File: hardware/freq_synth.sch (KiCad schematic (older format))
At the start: 13 parts

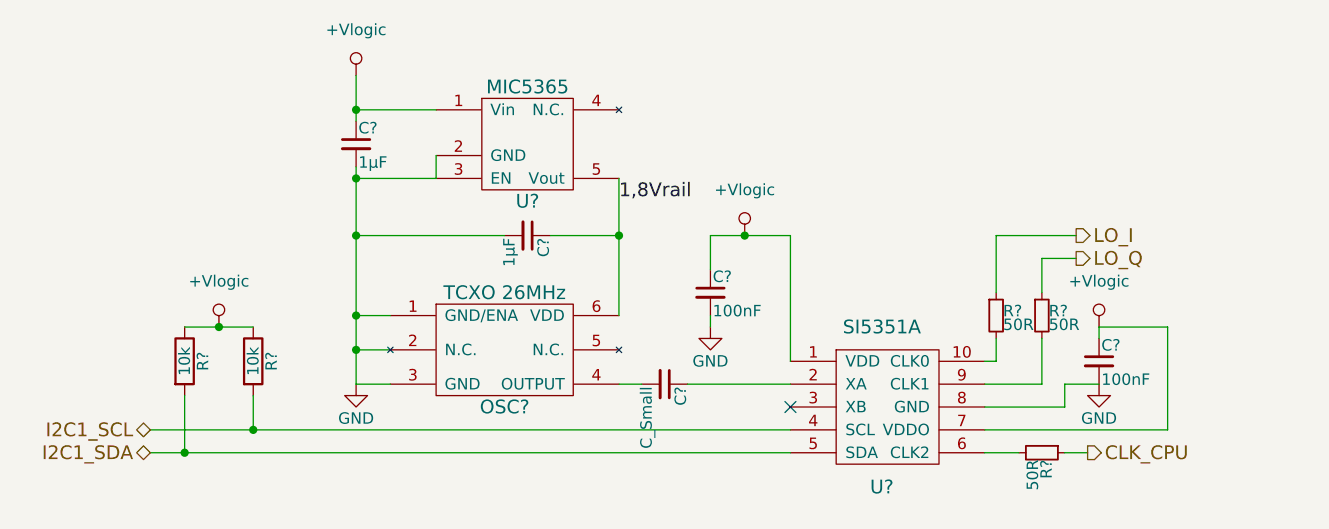
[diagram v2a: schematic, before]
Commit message: Added RX chain. also modified and cleand up other schemas
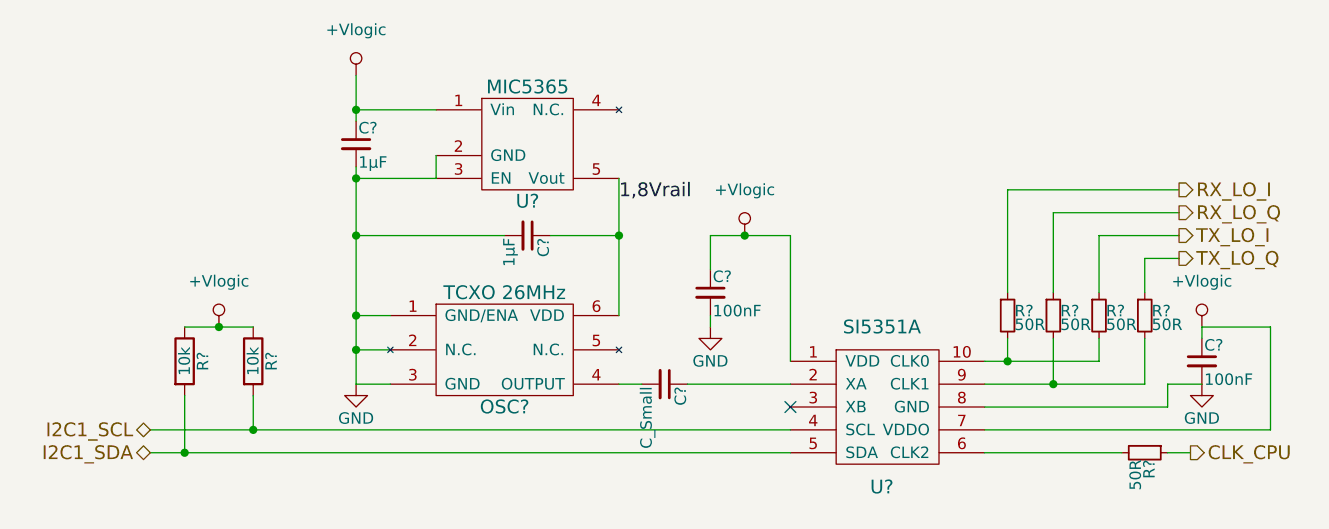
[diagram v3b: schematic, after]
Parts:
- added R? (x2): 50R, symbol R_Small
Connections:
- net at R?.2, U?.10 (CLK0): now also R?.2
- net at R?.2, U?.9 (CLK1): now also R?.2
- net LO_I renamed TX_LO_I
- net LO_Q renamed TX_LO_Q
- new net RX_LO_I: R?.1
- new net RX_LO_Q: R?.1
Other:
- moved on the sheet: C?, R?
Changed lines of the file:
@@
 $Descr A4 11693 8268
 encoding utf-8
-Sheet 2 5
+Sheet 2 7
 Title "Frequency synthesizer for LOs and CPU clock generation"
 Date "2016-09-22"
@@
 $EndDescr
 Wire Wire Line
-	7450 4500 7550 4500
-Wire Wire Line
-	7100 4500 7250 4500
-Wire Wire Line
-	7150 3550 7150 3800
-Wire Wire Line
-	7500 3550 7150 3550
-Wire Wire Line
-	7350 3650 7350 3800
-Wire Wire Line
-	7500 3650 7350 3650
-Wire Wire Line
-	7150 4100 7150 4000
-Wire Wire Line
-	7100 4100 7150 4100
-Wire Wire Line
-	7350 4200 7350 4000
-Wire Wire Line
-	7100 4200 7350 4200
+	7900 4500 8000 4500
+Wire Wire Line
+	7100 4500 7700 4500
+Wire Wire Line
+	7600 3550 7600 3800
+Wire Wire Line
+	7950 3550 7600 3550
+Wire Wire Line
+	7800 3650 7800 3800
+Wire Wire Line
+	7950 3650 7800 3650
+Wire Wire Line
+	7600 4100 7600 4000
+Wire Wire Line
+	7100 4100 7600 4100
+Wire Wire Line
+	7800 4200 7800 4000
+Wire Wire Line
+	7100 4200 7800 4200
 Connection ~ 3600 4500
 Connection ~ 3900 4400
 Wire Wire Line
-	7600 3950 7600 4000
-Wire Wire Line
-	7600 3950 7900 3950
-Wire Wire Line
-	7450 4200 7450 4300
+	8050 3950 8050 4000
+Wire Wire Line
+	8050 3950 8350 3950
+Wire Wire Line
+	7900 4200 7900 4300
 Connection ~ 4350 3000
 Connection ~ 4350 3550
 Wire Wire Line
-	5000 3550 4350 3550
+	4350 3550 5000 3550
 Connection ~ 5500 3550
 Wire Wire Line
@@
 	6250 3550 6250 4100
 Wire Wire Line
-	7900 3950 7900 4400
-Wire Wire Line
-	7900 4400 7100 4400
-Wire Wire Line
-	7450 4300 7100 4300
-Wire Wire Line
-	7450 4200 7600 4200
+	8350 3950 8350 4400
+Wire Wire Line
+	8350 4400 7100 4400
+Wire Wire Line
+	7900 4300 7100 4300
+Wire Wire Line
+	7900 4200 8050 4200
 Wire Wire Line
 	5900 3950 5900 3900
-Text HLabel 7550 4500 2    60   Output ~ 0
+Text HLabel 8000 4500 2    60   Output ~ 0
 CLK_CPU
 $Comp
 L R_Small R?
 U 1 1 57E319F9
-P 7350 4500
-F 0 "R?" H 7380 4520 50  0000 L CNN
-F 1 "50R" H 7380 4460 50  0000 L CNN
-F 2 "" H 7350 4500 50  0000 C CNN
-F 3 "" H 7350 4500 50  0000 C CNN
-	1    7350 4500
+P 7800 4500
+F 0 "R?" H 7830 4520 50  0000 L CNN
+F 1 "50R" H 7830 4460 50  0000 L CNN
+F 2 "" H 7800 4500 50  0000 C CNN
+F 3 "" H 7800 4500 50  0000 C CNN
+	1    7800 4500
 	0    1    1    0
 $EndComp
@@
 L R_Small R?
 U 1 1 57E31A00
-P 7150 3900
-F 0 "R?" H 7180 3920 50  0000 L CNN
-F 1 "50R" H 7180 3860 50  0000 L CNN
-F 2 "" H 7150 3900 50  0000 C CNN
-F 3 "" H 7150 3900 50  0000 C CNN
-	1    7150 3900
+P 7600 3900
+F 0 "R?" H 7630 3920 50  0000 L CNN
+F 1 "50R" H 7630 3860 50  0000 L CNN
+F 2 "" H 7600 3900 50  0000 C CNN
+F 3 "" H 7600 3900 50  0000 C CNN
+	1    7600 3900
 	1    0    0    -1
 $EndComp
@@
 L R_Small R?
 U 1 1 57E31A07
-P 7350 3900
-F 0 "R?" H 7380 3920 50  0000 L CNN
-F 1 "50R" H 7380 3860 50  0000 L CNN
-F 2 "" H 7350 3900 50  0000 C CNN
-F 3 "" H 7350 3900 50  0000 C CNN
-	1    7350 3900
-	1    0    0    -1
-$EndComp
-Text HLabel 7500 3550 2    60   Output ~ 0
-LO_I
-Text HLabel 7500 3650 2    60   Output ~ 0
-LO_Q
+P 7800 3900
+F 0 "R?" H 7830 3920 50  0000 L CNN
+F 1 "50R" H 7830 3860 50  0000 L CNN
+F 2 "" H 7800 3900 50  0000 C CNN
+F 3 "" H 7800 3900 50  0000 C CNN
+	1    7800 3900
+	1    0    0    -1
+$EndComp
+Text HLabel 7950 3550 2    60   Output ~ 0
+TX_LO_I
+Text HLabel 7950 3650 2    60   Output ~ 0
+TX_LO_Q
 Text HLabel 3450 4400 0    60   BiDi ~ 0
 I2C1_SCL
@@
 1,8Vrail
 $Comp
-L +Vlogic #PWR?
+L +Vlogic #PWR02
 U 1 1 57E31A13
 P 4350 2850
-F 0 "#PWR?" H 4350 2650 50  0001 C CNN
+F 0 "#PWR02" H 4350 2650 50  0001 C CNN
 F 1 "+Vlogic" H 4350 3050 50  0000 C CNN
 F 2 "" H 4350 2850 50  0000 C CNN
@@
 $EndComp
 $Comp
-L GND #PWR?
+L GND #PWR03
 U 1 1 57E31A2E
 P 4350 4200
-F 0 "#PWR?" H 4350 3950 50  0001 C CNN
+F 0 "#PWR03" H 4350 3950 50  0001 C CNN
 F 1 "GND" H 4350 4050 50  0000 C CNN
 F 2 "" H 4350 4200 50  0000 C CNN
@@
 $EndComp
 $Comp
-L +Vlogic #PWR?
+L +Vlogic #PWR04
 U 1 1 57E31A3B
 P 3750 3950
-F 0 "#PWR?" H 3750 3750 50  0001 C CNN
+F 0 "#PWR04" H 3750 3750 50  0001 C CNN
 F 1 "+Vlogic" H 3750 4150 50  0000 C CNN
 F 2 "" H 3750 3950 50  0000 C CNN
@@
 $EndComp
 $Comp
-L +Vlogic #PWR?
+L +Vlogic #PWR05
 U 1 1 57E31A41
-P 7600 3950
-F 0 "#PWR?" H 7600 3750 50  0001 C CNN
-F 1 "+Vlogic" H 7600 4150 50  0000 C CNN
-F 2 "" H 7600 3950 50  0000 C CNN
-F 3 "" H 7600 3950 50  0000 C CNN
-	1    7600 3950
+P 8050 3950
+F 0 "#PWR05" H 8050 3750 50  0001 C CNN
+F 1 "+Vlogic" H 8050 4150 50  0000 C CNN
+F 2 "" H 8050 3950 50  0000 C CNN
+F 3 "" H 8050 3950 50  0000 C CNN
+	1    8050 3950
 	1    0    0    -1
 $EndComp
@@
 $EndComp
 $Comp
-L +Vlogic #PWR?
+L +Vlogic #PWR06
 U 1 1 57E31A5D
 P 6050 3550
-F 0 "#PWR?" H 6050 3350 50  0001 C CNN
+F 0 "#PWR06" H 6050 3350 50  0001 C CNN
 F 1 "+Vlogic" H 6050 3750 50  0000 C CNN
 F 2 "" H 6050 3550 50  0000 C CNN
@@
 L C_Small C?
 U 1 1 57E31A63
-P 7600 4100
-F 0 "C?" H 7610 4170 50  0000 L CNN
-F 1 "100nF" H 7610 4020 50  0000 L CNN
-F 2 "" H 7600 4100 50  0000 C CNN
-F 3 "" H 7600 4100 50  0000 C CNN
-	1    7600 4100
+P 8050 4100
+F 0 "C?" H 8060 4170 50  0000 L CNN
+F 1 "100nF" H 8060 4020 50  0000 L CNN
+F 2 "" H 8050 4100 50  0000 C CNN
+F 3 "" H 8050 4100 50  0000 C CNN
+	1    8050 4100
 	1    0    0    -1
 $EndComp
@@
 $EndComp
 $Comp
-L GND #PWR?
+L GND #PWR07
 U 1 1 57E31A71
 P 5900 3950
-F 0 "#PWR?" H 5900 3700 50  0001 C CNN
+F 0 "#PWR07" H 5900 3700 50  0001 C CNN
 F 1 "GND" H 5900 3800 50  0000 C CNN
 F 2 "" H 5900 3950 50  0000 C CNN
@@
 $EndComp
 $Comp
-L GND #PWR?
+L GND #PWR08
 U 1 1 57E31A77
-P 7600 4200
-F 0 "#PWR?" H 7600 3950 50  0001 C CNN
-F 1 "GND" H 7600 4050 50  0000 C CNN
-F 2 "" H 7600 4200 50  0000 C CNN
-F 3 "" H 7600 4200 50  0000 C CNN
-	1    7600 4200
+P 8050 4200
+F 0 "#PWR08" H 8050 3950 50  0001 C CNN
+F 1 "GND" H 8050 4050 50  0000 C CNN
+F 2 "" H 8050 4200 50  0000 C CNN
+F 3 "" H 8050 4200 50  0000 C CNN
+	1    8050 4200
 	1    0    0    -1
 $EndComp
@@
 	1    0    0    -1
 $EndComp
+$Comp
+L R_Small R?
+U 1 1 57E545D0
+P 7400 3900
+F 0 "R?" H 7430 3920 50  0000 L CNN
+F 1 "50R" H 7430 3860 50  0000 L CNN
+F 2 "" H 7400 3900 50  0000 C CNN
+F 3 "" H 7400 3900 50  0000 C CNN
+	1    7400 3900
+	1    0    0    -1
+$EndComp
+$Comp
+L R_Small R?
+U 1 1 57E54652
+P 7200 3900
+F 0 "R?" H 7230 3920 50  0000 L CNN
+F 1 "50R" H 7230 3860 50  0000 L CNN
+F 2 "" H 7200 3900 50  0000 C CNN
+F 3 "" H 7200 3900 50  0000 C CNN
+	1    7200 3900
+	1    0    0    -1
+$EndComp
+Wire Wire Line
+	7200 4100 7200 4000
+Connection ~ 7200 4100
+Wire Wire Line
+	7400 4200 7400 4000
+Connection ~ 7400 4200
+Text HLabel 7950 3450 2    60   Output ~ 0
+RX_LO_Q
+Text HLabel 7950 3350 2    60   Output ~ 0
+RX_LO_I
+Wire Wire Line
+	7400 3800 7400 3450
+Wire Wire Line
+	7400 3450 7950 3450
+Wire Wire Line
+	7200 3800 7200 3350
+Wire Wire Line
+	7200 3350 7950 3350
 $EndSCHEMATC

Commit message: Added annotation so willing prove readers can reference components more easily
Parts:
- gave numbers to parts that had none: 15
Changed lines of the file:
@@
 CLK_CPU
 $Comp
-L R_Small R?
+L R_Small R207
 U 1 1 57E319F9
 P 7800 4500
-F 0 "R?" H 7830 4520 50  0000 L CNN
+F 0 "R207" H 7830 4520 50  0000 L CNN
 F 1 "50R" H 7830 4460 50  0000 L CNN
 F 2 "" H 7800 4500 50  0000 C CNN
@@
 $EndComp
 $Comp
-L R_Small R?
+L R_Small R205
 U 1 1 57E31A00
 P 7600 3900
-F 0 "R?" H 7630 3920 50  0000 L CNN
+F 0 "R205" H 7630 3920 50  0000 L CNN
 F 1 "50R" H 7630 3860 50  0000 L CNN
 F 2 "" H 7600 3900 50  0000 C CNN
@@
 $EndComp
 $Comp
-L R_Small R?
+L R_Small R206
 U 1 1 57E31A07
 P 7800 3900
-F 0 "R?" H 7830 3920 50  0000 L CNN
+F 0 "R206" H 7830 3920 50  0000 L CNN
 F 1 "50R" H 7830 3860 50  0000 L CNN
 F 2 "" H 7800 3900 50  0000 C CNN
@@
 1,8Vrail
 $Comp
-L +Vlogic #PWR02
+L +Vlogic #PWR202
 U 1 1 57E31A13
 P 4350 2850
-F 0 "#PWR02" H 4350 2650 50  0001 C CNN
+F 0 "#PWR202" H 4350 2650 50  0001 C CNN
 F 1 "+Vlogic" H 4350 3050 50  0000 C CNN
 F 2 "" H 4350 2850 50  0000 C CNN
@@
 $EndComp
 $Comp
-L C_Small C?
+L C_Small C202
 U 1 1 57E31A19
 P 5100 3550
-F 0 "C?" H 5110 3620 50  0000 L CNN
+F 0 "C202" H 5110 3620 50  0000 L CNN
 F 1 "1µF" H 5110 3470 50  0000 L CNN
 F 2 "" H 5100 3550 50  0000 C CNN
@@
 $EndComp
 $Comp
-L C_Small C?
+L C_Small C201
 U 1 1 57E31A20
 P 4350 3150
-F 0 "C?" H 4360 3220 50  0000 L CNN
+F 0 "C201" H 4360 3220 50  0000 L CNN
 F 1 "1µF" H 4360 3070 50  0000 L CNN
 F 2 "" H 4350 3150 50  0000 C CNN
@@
 $EndComp
 $Comp
-L LDO U?
+L LDO U201
 U 1 1 57E31A27
 P 5100 3100
-F 0 "U?" H 5100 2800 60  0000 C CNN
+F 0 "U201" H 5100 2800 60  0000 C CNN
 F 1 "MIC5365" H 5100 3300 60  0000 C CNN
 F 2 "" H 5100 3050 60  0001 C CNN
@@
 $EndComp
 $Comp
-L GND #PWR03
+L GND #PWR203
 U 1 1 57E31A2E
 P 4350 4200
-F 0 "#PWR03" H 4350 3950 50  0001 C CNN
+F 0 "#PWR203" H 4350 3950 50  0001 C CNN
 F 1 "GND" H 4350 4050 50  0000 C CNN
 F 2 "" H 4350 4200 50  0000 C CNN
@@
 $EndComp
 $Comp
-L TCXO OSC?
+L TCXO OSC201
 U 1 1 57E31A34
 P 5000 4050
-F 0 "OSC?" H 5000 3800 60  0000 C CNN
+F 0 "OSC201" H 5000 3800 60  0000 C CNN
 F 1 "TCXO 26MHz" H 5000 4300 60  0000 C CNN
 F 2 "" H 5050 4150 60  0001 C CNN
@@
 $EndComp
 $Comp
-L +Vlogic #PWR04
+L +Vlogic #PWR201
 U 1 1 57E31A3B
 P 3750 3950
-F 0 "#PWR04" H 3750 3750 50  0001 C CNN
+F 0 "#PWR201" H 3750 3750 50  0001 C CNN
 F 1 "+Vlogic" H 3750 4150 50  0000 C CNN
 F 2 "" H 3750 3950 50  0000 C CNN
@@
 $EndComp
 $Comp
-L +Vlogic #PWR05
+L +Vlogic #PWR206
 U 1 1 57E31A41
 P 8050 3950
-F 0 "#PWR05" H 8050 3750 50  0001 C CNN
+F 0 "#PWR206" H 8050 3750 50  0001 C CNN
 F 1 "+Vlogic" H 8050 4150 50  0000 C CNN
 F 2 "" H 8050 3950 50  0000 C CNN
@@
 $EndComp
 $Comp
-L R R?
+L R R201
 U 1 1 57E31A47
 P 3600 4100
-F 0 "R?" V 3680 4100 50  0000 C CNN
+F 0 "R201" V 3680 4100 50  0000 C CNN
 F 1 "10k" V 3600 4100 50  0000 C CNN
 F 2 "" V 3530 4100 50  0000 C CNN
@@
 $EndComp
 $Comp
-L R R?
+L R R202
 U 1 1 57E31A4E
 P 3900 4100
-F 0 "R?" V 3980 4100 50  0000 C CNN
+F 0 "R202" V 3980 4100 50  0000 C CNN
 F 1 "10k" V 3900 4100 50  0000 C CNN
 F 2 "" V 3830 4100 50  0000 C CNN
@@
 NoConn ~ 6250 4300
 $Comp
-L C_Small C?
+L C_Small C203
 U 1 1 57E31A56
 P 5700 4200
-F 0 "C?" H 5710 4270 50  0000 L CNN
+F 0 "C203" H 5710 4270 50  0000 L CNN
 F 1 "C_Small" H 5710 4120 50  0000 L CNN
 F 2 "" H 5700 4200 50  0000 C CNN
@@
 $EndComp
 $Comp
-L +Vlogic #PWR06
+L +Vlogic #PWR205
 U 1 1 57E31A5D
 P 6050 3550
-F 0 "#PWR06" H 6050 3350 50  0001 C CNN
+F 0 "#PWR205" H 6050 3350 50  0001 C CNN
 F 1 "+Vlogic" H 6050 3750 50  0000 C CNN
 F 2 "" H 6050 3550 50  0000 C CNN
@@
 $EndComp
 $Comp
-L C_Small C?
+L C_Small C205
 U 1 1 57E31A63
 P 8050 4100
-F 0 "C?" H 8060 4170 50  0000 L CNN
+F 0 "C205" H 8060 4170 50  0000 L CNN
 F 1 "100nF" H 8060 4020 50  0000 L CNN
 F 2 "" H 8050 4100 50  0000 C CNN
@@
 $EndComp
 $Comp
-L C_Small C?
+L C_Small C204
 U 1 1 57E31A6A
 P 5900 3800
-F 0 "C?" H 5910 3870 50  0000 L CNN
+F 0 "C204" H 5910 3870 50  0000 L CNN
 F 1 "100nF" H 5910 3720 50  0000 L CNN
 F 2 "" H 5900 3800 50  0000 C CNN
@@
 $EndComp
 $Comp
-L GND #PWR07
+L GND #PWR204
 U 1 1 57E31A71
 P 5900 3950
-F 0 "#PWR07" H 5900 3700 50  0001 C CNN
+F 0 "#PWR204" H 5900 3700 50  0001 C CNN
 F 1 "GND" H 5900 3800 50  0000 C CNN
 F 2 "" H 5900 3950 50  0000 C CNN
@@
 $EndComp
 $Comp
-L GND #PWR08
+L GND #PWR207
 U 1 1 57E31A77
 P 8050 4200
-F 0 "#PWR08" H 8050 3950 50  0001 C CNN
+F 0 "#PWR207" H 8050 3950 50  0001 C CNN
 F 1 "GND" H 8050 4050 50  0000 C CNN
 F 2 "" H 8050 4200 50  0000 C CNN
@@
 $EndComp
 $Comp
-L SI5351A U?
+L SI5351A U202
 U 1 1 57E31A7D
 P 6650 4300
-F 0 "U?" H 6650 3950 60  0000 C CNN
+F 0 "U202" H 6650 3950 60  0000 C CNN
 F 1 "SI5351A" H 6650 4650 60  0000 C CNN
 F 2 "" H 6650 4650 60  0001 C CNN
@@
 $EndComp
 $Comp
-L R_Small R?
+L R_Small R204
 U 1 1 57E545D0
 P 7400 3900
-F 0 "R?" H 7430 3920 50  0000 L CNN
+F 0 "R204" H 7430 3920 50  0000 L CNN
 F 1 "50R" H 7430 3860 50  0000 L CNN
 F 2 "" H 7400 3900 50  0000 C CNN
@@
 $EndComp
 $Comp
-L R_Small R?
+L R_Small R203
 U 1 1 57E54652
 P 7200 3900
-F 0 "R?" H 7230 3920 50  0000 L CNN
+F 0 "R203" H 7230 3920 50  0000 L CNN
 F 1 "50R" H 7230 3860 50  0000 L CNN
 F 2 "" H 7200 3900 50  0000 C CNN

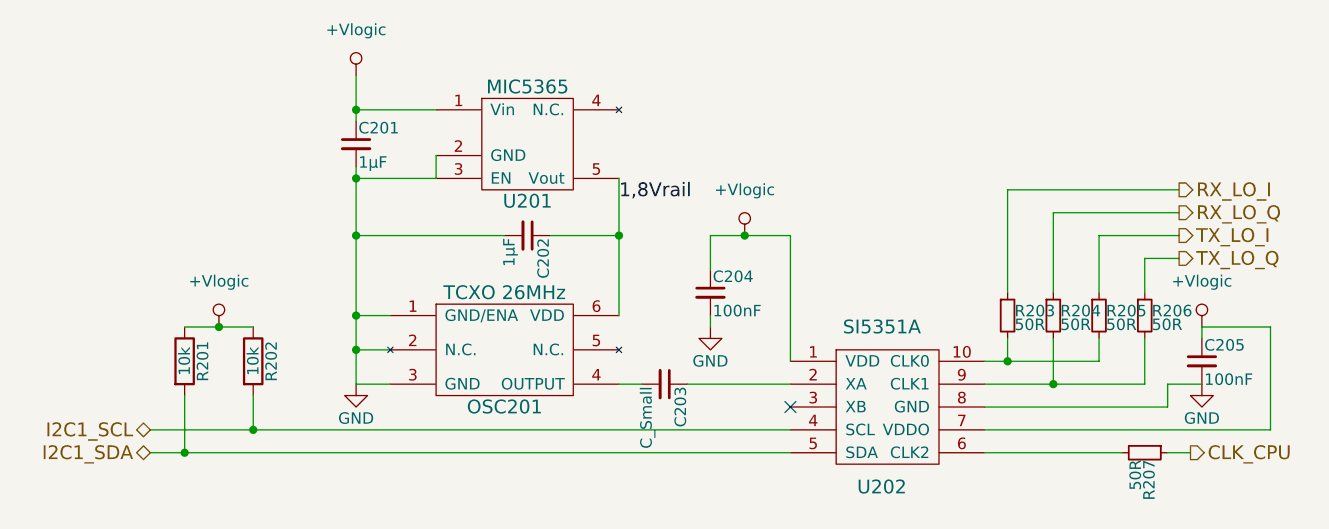
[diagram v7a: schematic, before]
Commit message: fixed some more ERC errors
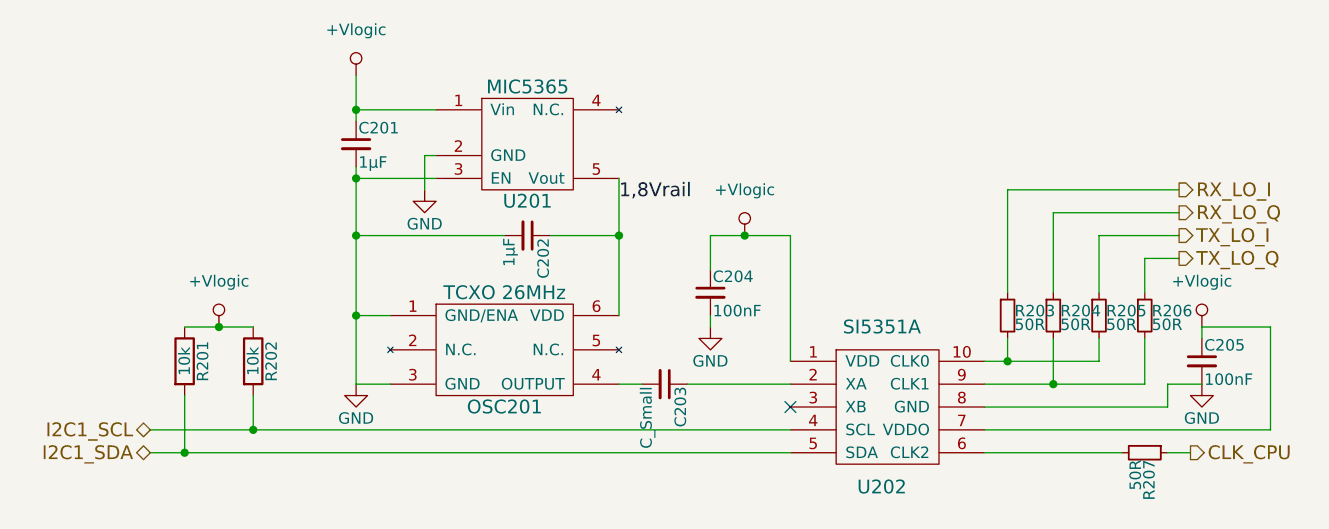
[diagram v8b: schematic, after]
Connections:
- net GND: no longer OSC201.2 (N.C.)
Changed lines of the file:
@@
 	4700 3300 4350 3300
-Wire Wire Line
-	4700 3200 4700 3300
 Wire Wire Line
 	4350 3250 4350 4200
@@
 Wire Wire Line
 	4350 4200 4500 4200
-Connection ~ 4350 4050
-Wire Wire Line
-	4350 4050 4500 4050
 Wire Wire Line
 	4350 3900 4500 3900
@@
 1,8Vrail
 $Comp
-L +Vlogic #PWR03
+L +Vlogic #PWR05
 U 1 1 57E31A13
 P 4350 2850
-F 0 "#PWR03" H 4350 2650 50  0001 C CNN
+F 0 "#PWR05" H 4350 2650 50  0001 C CNN
 F 1 "+Vlogic" H 4350 3050 50  0000 C CNN
 F 2 "" H 4350 2850 50  0000 C CNN
@@
 $EndComp
 $Comp
-L GND #PWR04
+L GND #PWR06
 U 1 1 57E31A2E
 P 4350 4200
-F 0 "#PWR04" H 4350 3950 50  0001 C CNN
+F 0 "#PWR06" H 4350 3950 50  0001 C CNN
 F 1 "GND" H 4350 4050 50  0000 C CNN
 F 2 "" H 4350 4200 50  0000 C CNN
@@
 $EndComp
 $Comp
-L +Vlogic #PWR05
+L +Vlogic #PWR07
 U 1 1 57E31A3B
 P 3750 3950
-F 0 "#PWR05" H 3750 3750 50  0001 C CNN
+F 0 "#PWR07" H 3750 3750 50  0001 C CNN
 F 1 "+Vlogic" H 3750 4150 50  0000 C CNN
 F 2 "" H 3750 3950 50  0000 C CNN
@@
 $EndComp
 $Comp
-L +Vlogic #PWR06
+L +Vlogic #PWR08
 U 1 1 57E31A41
 P 8050 3950
-F 0 "#PWR06" H 8050 3750 50  0001 C CNN
+F 0 "#PWR08" H 8050 3750 50  0001 C CNN
 F 1 "+Vlogic" H 8050 4150 50  0000 C CNN
 F 2 "" H 8050 3950 50  0000 C CNN
@@
 $EndComp
 $Comp
-L +Vlogic #PWR07
+L +Vlogic #PWR09
 U 1 1 57E31A5D
 P 6050 3550
-F 0 "#PWR07" H 6050 3350 50  0001 C CNN
+F 0 "#PWR09" H 6050 3350 50  0001 C CNN
 F 1 "+Vlogic" H 6050 3750 50  0000 C CNN
 F 2 "" H 6050 3550 50  0000 C CNN
@@
 $EndComp
 $Comp
-L GND #PWR08
+L GND #PWR010
 U 1 1 57E31A71
 P 5900 3950
-F 0 "#PWR08" H 5900 3700 50  0001 C CNN
+F 0 "#PWR010" H 5900 3700 50  0001 C CNN
 F 1 "GND" H 5900 3800 50  0000 C CNN
 F 2 "" H 5900 3950 50  0000 C CNN
@@
 $EndComp
 $Comp
-L GND #PWR09
+L GND #PWR011
 U 1 1 57E31A77
 P 8050 4200
-F 0 "#PWR09" H 8050 3950 50  0001 C CNN
+F 0 "#PWR011" H 8050 3950 50  0001 C CNN
 F 1 "GND" H 8050 4050 50  0000 C CNN
 F 2 "" H 8050 4200 50  0000 C CNN
@@
 Wire Wire Line
 	7200 3350 7950 3350
+$Comp
+L GND #PWR012
+U 1 1 57EDA76C
+P 4650 3350
+F 0 "#PWR012" H 4650 3100 50  0001 C CNN
+F 1 "GND" H 4650 3200 50  0000 C CNN
+F 2 "" H 4650 3350 50  0000 C CNN
+F 3 "" H 4650 3350 50  0000 C CNN
+	1    4650 3350
+	1    0    0    -1
+$EndComp
+Wire Wire Line
+	4700 3200 4650 3200
+Wire Wire Line
+	4650 3200 4650 3350
 $EndSCHEMATC
